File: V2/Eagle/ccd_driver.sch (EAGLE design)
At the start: 117 parts, among them J3 POWER_JACK, Q1 1A/60V/2.4Ω, Q2 BC214, Q3 2N2222, U10 TPD4S012DRYR, U11 0ZCJ0050FF2G, U12 REF3025AIDBZR, U13 DMP6023LE-13, U14 LMR23630, U2 MK02FN128VLF10, U4 ADS7946SRTER, U5 CP2102N-A01-GQFN20R, U8 S602TSRP

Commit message: modified power supply again. Added filter, ldo, and charge pump for analog rails. Created new schematic frame. General organization and minor changes
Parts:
- removed C110: 10uF, rcl:C-EUC0805
- removed C61, C62, C77: 100nF, SparkFun-Capacitors:10PF-50V-5%(0603)
- removed C69: 2.2uF, SparkFun-Capacitors:10PF-50V-5%(0603)
- removed C79: UWZ1C151MCL1GS, caps:UWZ1C151MCL1GS
- removed C88: 10uF, SparkFun-Capacitors:10PF-50V-5%(0603)
- removed C92: 47 pF, SparkFun-Capacitors:10PF-50V-5%(0603)
- removed C99: EMVE160ADA101MF55G, LM2776DBVR:EMVE160ADA101MF55G
- removed F3: 2920PTC, fuses:2920PTC
- removed J3: POWER_JACK, SparkFun-Connectors:POWER_JACK
- removed U12: REF3025AIDBZR, REF3025_DBZ-3:REF3025AIDBZR
- removed U8: S602TSRP, fuses:BT168GW
- added C18, C19, C25, C30, C45, C46, C48, C54: 10uF, eagle-ltspice:CC1206
- added C20, C21, C27, C35: 100nF, SparkFun-Capacitors:10PF-50V-5%(0603)
- added C22, C38, C53: UWZ1C151MCL1GS, caps:UWZ1C151MCL1GS
- added C24, C55: 1uF, SparkFun-Capacitors:10PF-50V-5%(0603)
- added C26, C28, C29, C33, C47: 2.2uF, rcl:C-EUC0805
- added C32: 10uF, SparkFun-Capacitors:10PF-50V-5%(0603)
- added C34: 10uF, rcl:C-EUC0805
- added C39: 0.47uF, SparkFun-Capacitors:10PF-50V-5%(0603)
- added C40: 4.7uF, SparkFun-Capacitors:10PF-50V-5%(0603)
- added C41: 2.2uF, SparkFun-Capacitors:10PF-50V-5%(0603)
- added C43: UWT1H101MNL1GS, UWT1H101MNL1GS:UWT1H101MNL1GS
- added C49, C50: EMVE160ADA101MF55G, caps:UWZ1C151MCL1GS
- added C51, C52, C56: 22uF, rcl:C-EUC0805
- added F5: 2920PTC, fuses:2920PTC
- added JACK1: JACK-C-PC-10A-RA(R), con-dcjack:JACK-C-PC-10A-RA(R)
- added JP4: (no value), pinhead:PINHD-1X2
- added L3: CIGW252010GLR47MNE, LM2776DBVR:CIGW252010GLR47MNE
- added R32, R47: 0, audio amplifier example:R-US_R0603
- added R33, R34: 51k, audio amplifier example:R-US_R0603
- added SUPPLY21: 2PT_GND_TIE, SparkFun-PowerSymbols:2PT_GND_TIE
- added T2: BC846, transistor:BC846
- added TP2: TPPAD1-13, testpad:TPPAD1-13
- added U$: LM2776DBVR, LM2776DBVR:LM2776DBVR
- added U1: S602TSRP, fuses:BT168GW
- added U3: REF3025AIDBZR, REF3025_DBZ-3:REF3025AIDBZR
- added U6: L5150BNTR, L5150BNTR:L5150BNTR
- C17: value 10uF -> UWT1H101MNL1GS; device eagle-ltspice:CC1206 -> UWT1H101MNL1GS:UWT1H101MNL1GS; CAPACITANCE (none) -> 100uF; PARTNO 490-12456-1-ND -> (none)
- CR1: ESD (none) -> 30kV; PEAKPOWER (none) -> 400W
- F6: IHOLD 1A -> 3A; PARTNO 2920L100 -> 2920L300
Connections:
- removed net N$25: F3.P$1, U13.D
- removed net N$5: C17.1, D4.A, R31.2, U8.G
- new net N$27: F5.P$1, U13.D
- new net N$34: C19.1, D4.A, R31.2, U1.G
- new net N$35: C45.1, R32.1, U6.IN
- new net N$36: L3.2, R32.2
- new net N$38: C25.1, R33.1, R34.2, T2.B
- new net N$39: C27.1, L3.1, T2.E
- new net N$4: C17.11, CR1.2, F5.P$2, JP4.2
- new net N$67: C48.1, R47.1, R54.1, U14.VIN
- new net N$93: C24.1, U$.C1+
- new net N$94: C24.2, U$.C1-
- new net V+: C20.1, C28.1, C29.1, C46.1, U$.EN, U$.VIN, U3.IN, U6.OUT
- new net V-: C26.1, U$.VOUT
- net +VIN: now also C18.1, C43.11, R33.2, R47.2, T2.C, U1.A; no longer C110.1, R54.1, U14.VIN, U8.A
- net 3.3V: now also R51.1; no longer C61.1, U12.IN
- net AGND: now also C20.2, C21.2, C26.2, C28.2, C29.2, C45.2, C46.2, SUPPLY21.P$1, U$.GND, U3.GND, U6.GND
- net GND: now also C17.22, C18.2, C19.2, C22.22, C25.2, C27.2, C33.2, C43.22, C48.2, C49.22, C51.2, C52.2, JACK1.2, R34.1, SUPPLY21.P$2, U1.K; no longer C110.2, C17.2, C61.2, C62.2, C69.2, C77.2, C79.22, C88.2, C99.11, J3.GND, J3.GNDBREAK, U12.GND, U8.K
- net N$14: now also JACK1.1, JP4.1, TP2.TP; no longer CR1.2, F3.P$2, J3.PWR
- net N$61: now also C33.1; no longer C69.1
- net N$70: no longer C92.2
- net N$88: now also C22.11, C51.1, C52.1; no longer C77.1, C79.11, C88.1, C92.1, R51.1
- net N$95: now also C49.11; no longer C99.22
- net VREF: now also C21.1, U3.OUT; no longer C62.1, U12.OUT
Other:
- note added: "+2.5V Ref"
- note added: "+5VA"
- note added: "-5VA"
- note added: "1.8" TFT Screen"
- note added: "3.3V Buck"
- note added: "5-36V Jack Input"
- note added: "Each peltier is seperatly fuesd"
- note added: "Encoder with pushbutton and LEDs"
- note added: "RC Filter W/ Bypass Transistor"
- note added: "Star Grounding"
- note added: "TODO: Add low ripple analog voltage [X]"
- note added: "TODO: Add negative rail [X]"
- note added: "TODO: Cosoldate all nets, pick pins on microcontroller"
- note added: "TODO: Fix amplifier, add unity gain amp, add filters"
- note added: "USB-B Micro"
- note removed: "5-36V Tolerant Input, 3.3V Out"
- note removed: "CCD & Amp"
- note removed: "CCD + AMP"
- note removed: "Main Microcontroller"
- note removed: "Peltier Cooler Driver"
- note removed: "Peltier Cooler Driver + Thermistor + Fan"
- note removed: "Power"
- note removed: "Precision 3V voltage ref"
- note removed: "SD Card"
- note removed: "TFT Screen + Encoder"
- note removed: "TFT-Screen + Encoder"
- note removed: "TODO: Add low ripple analog voltage"
- note removed: "TODO: Add negative rail"
- note removed: "TODO: Fix amplifier, add unity gain amp"
- note removed: "USB"

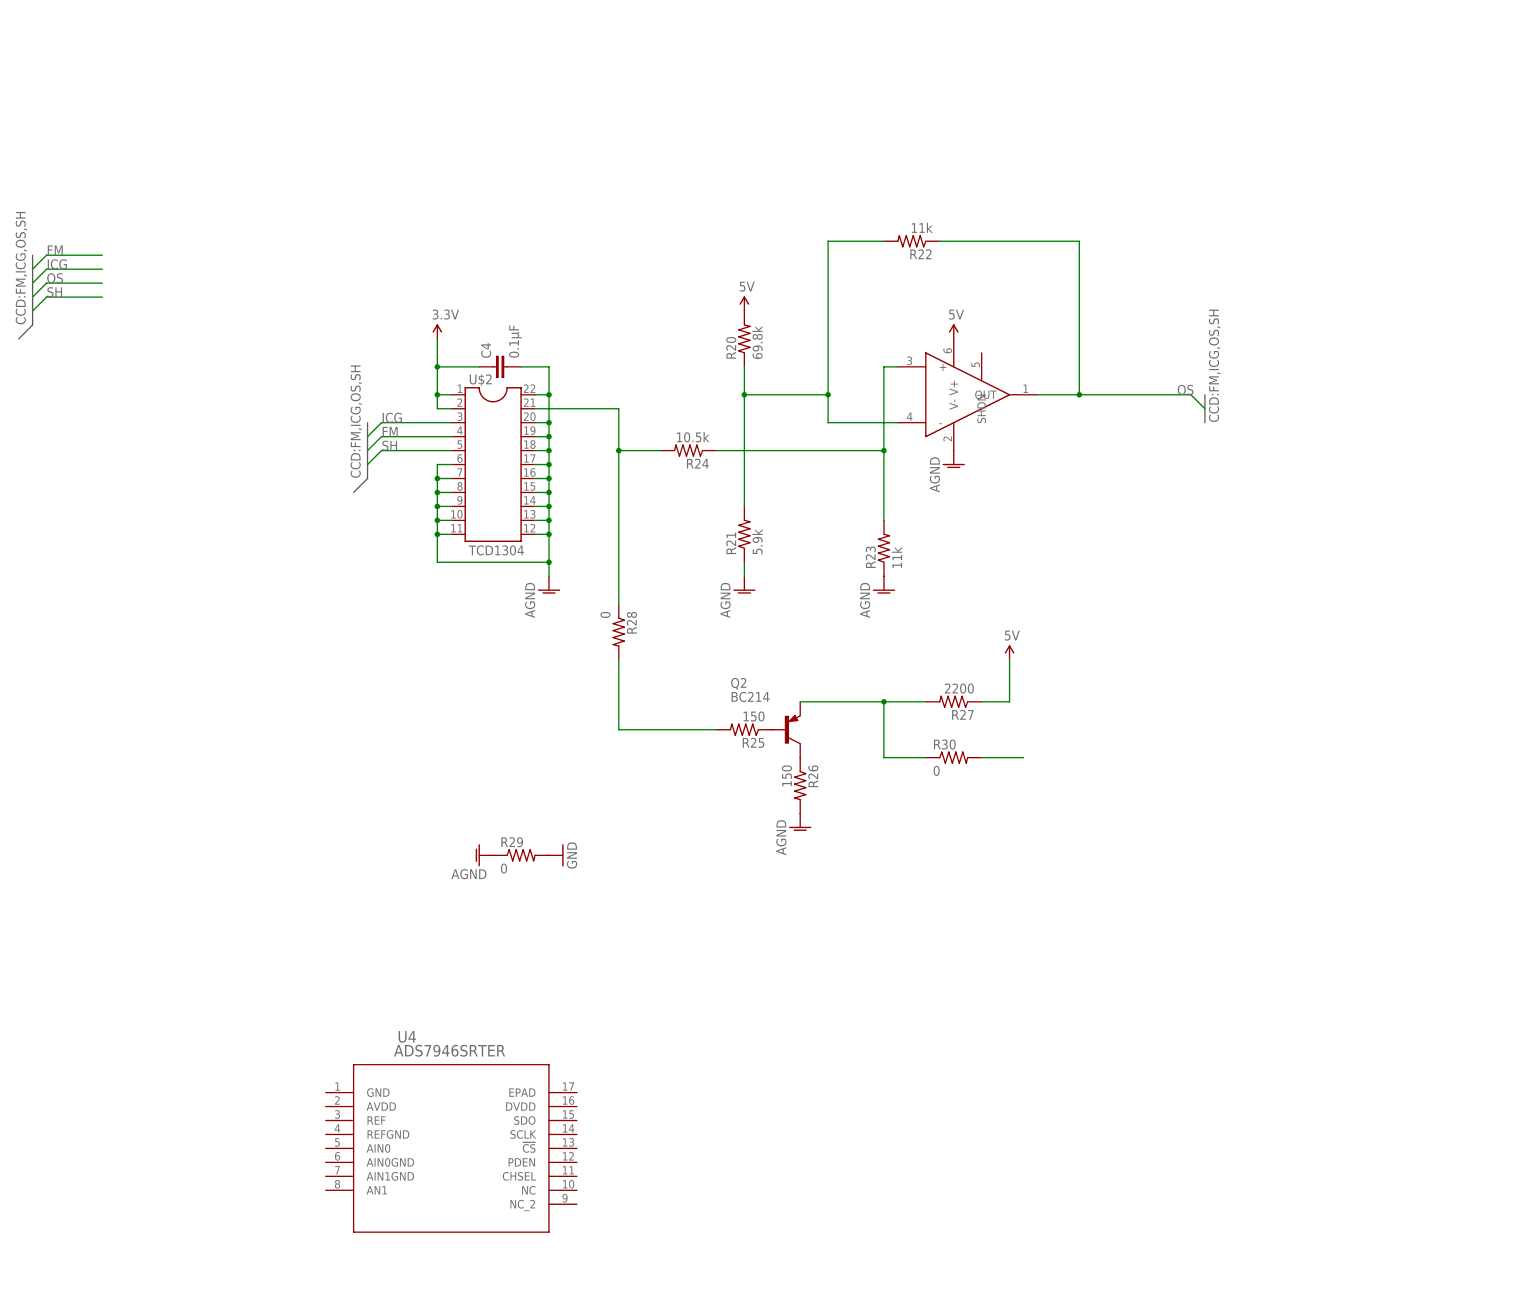
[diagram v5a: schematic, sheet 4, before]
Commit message: made matlab script to autocalculate amplifier resistor values
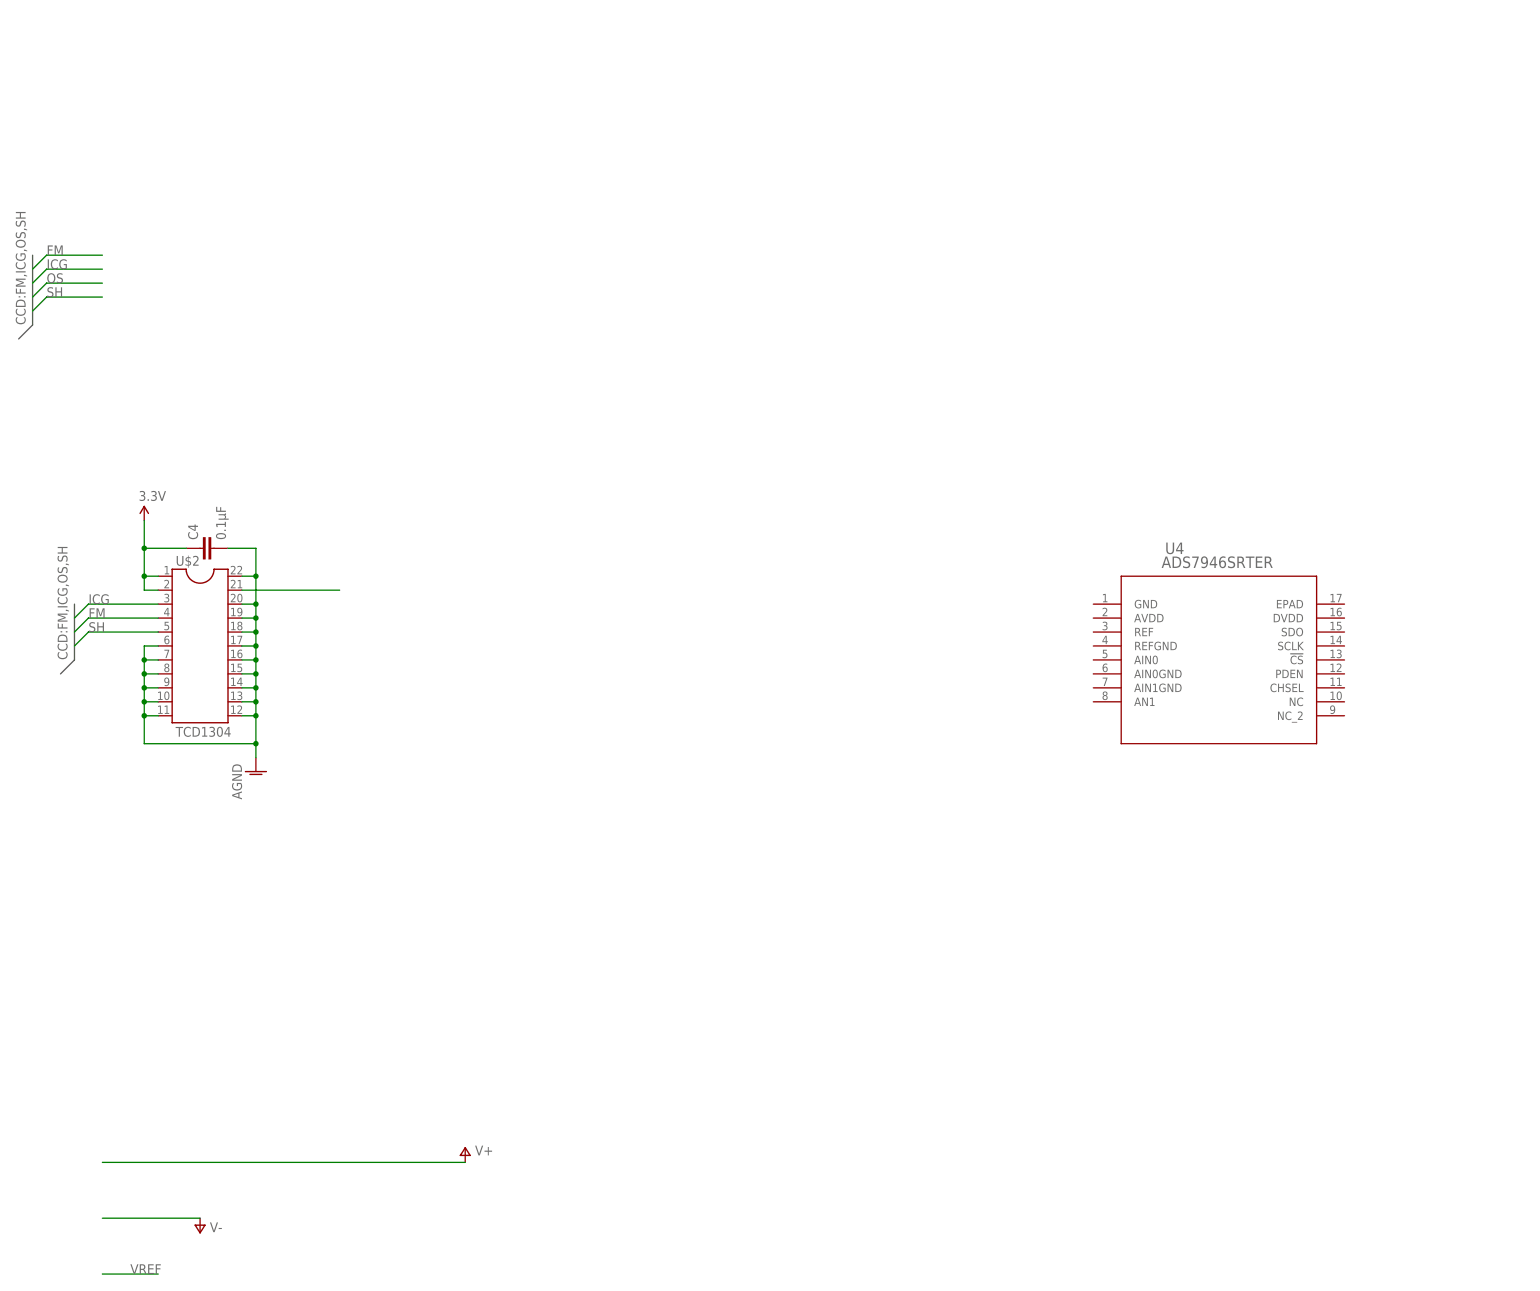
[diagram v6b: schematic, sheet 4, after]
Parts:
- removed Q2: BC214, transistor-pnp:BC214
- removed R20: 69.8k, resistor:R-US_R0805
- removed R21: 5.9k, resistor:R-US_R0805
- removed R22, R23: 11k, resistor:R-US_R0805
- removed R24: 10.5k, resistor:R-US_R0805
- removed R25, R26: 150, resistor:R-US_R0805
- removed R27: 2200, resistor:R-US_R0805
- removed R28, R29, R30: 0, resistor:R-US_R0805
- removed U$5: LTC6252, ccd:LTC6252
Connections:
- removed net 5V: R20.2, R27.1, U$5.V+
- removed net BU1: Q2.E, R27.2, R30.1
- removed net N$28: R23.2, R24.1, U$5.+
- removed net N$29: R24.2, R28.1, U$2.21
- removed net N$30: Q2.B, R25.1
- removed net N$31: Q2.C, R26.1
- removed net N$32: R25.2, R28.2
- removed net N$6: R20.1, R21.2, R22.2, U$5.-
- removed net OS: R22.1, R30.2, U$5.OUT
- new net N$5: U$2.21
- net AGND: no longer R21.1, R23.1, R26.2, R29.1, U$5.V-
- net GND: no longer R29.2
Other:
- moved on the sheet: C4, U$2, U4

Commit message: added new amp circuit for CCD
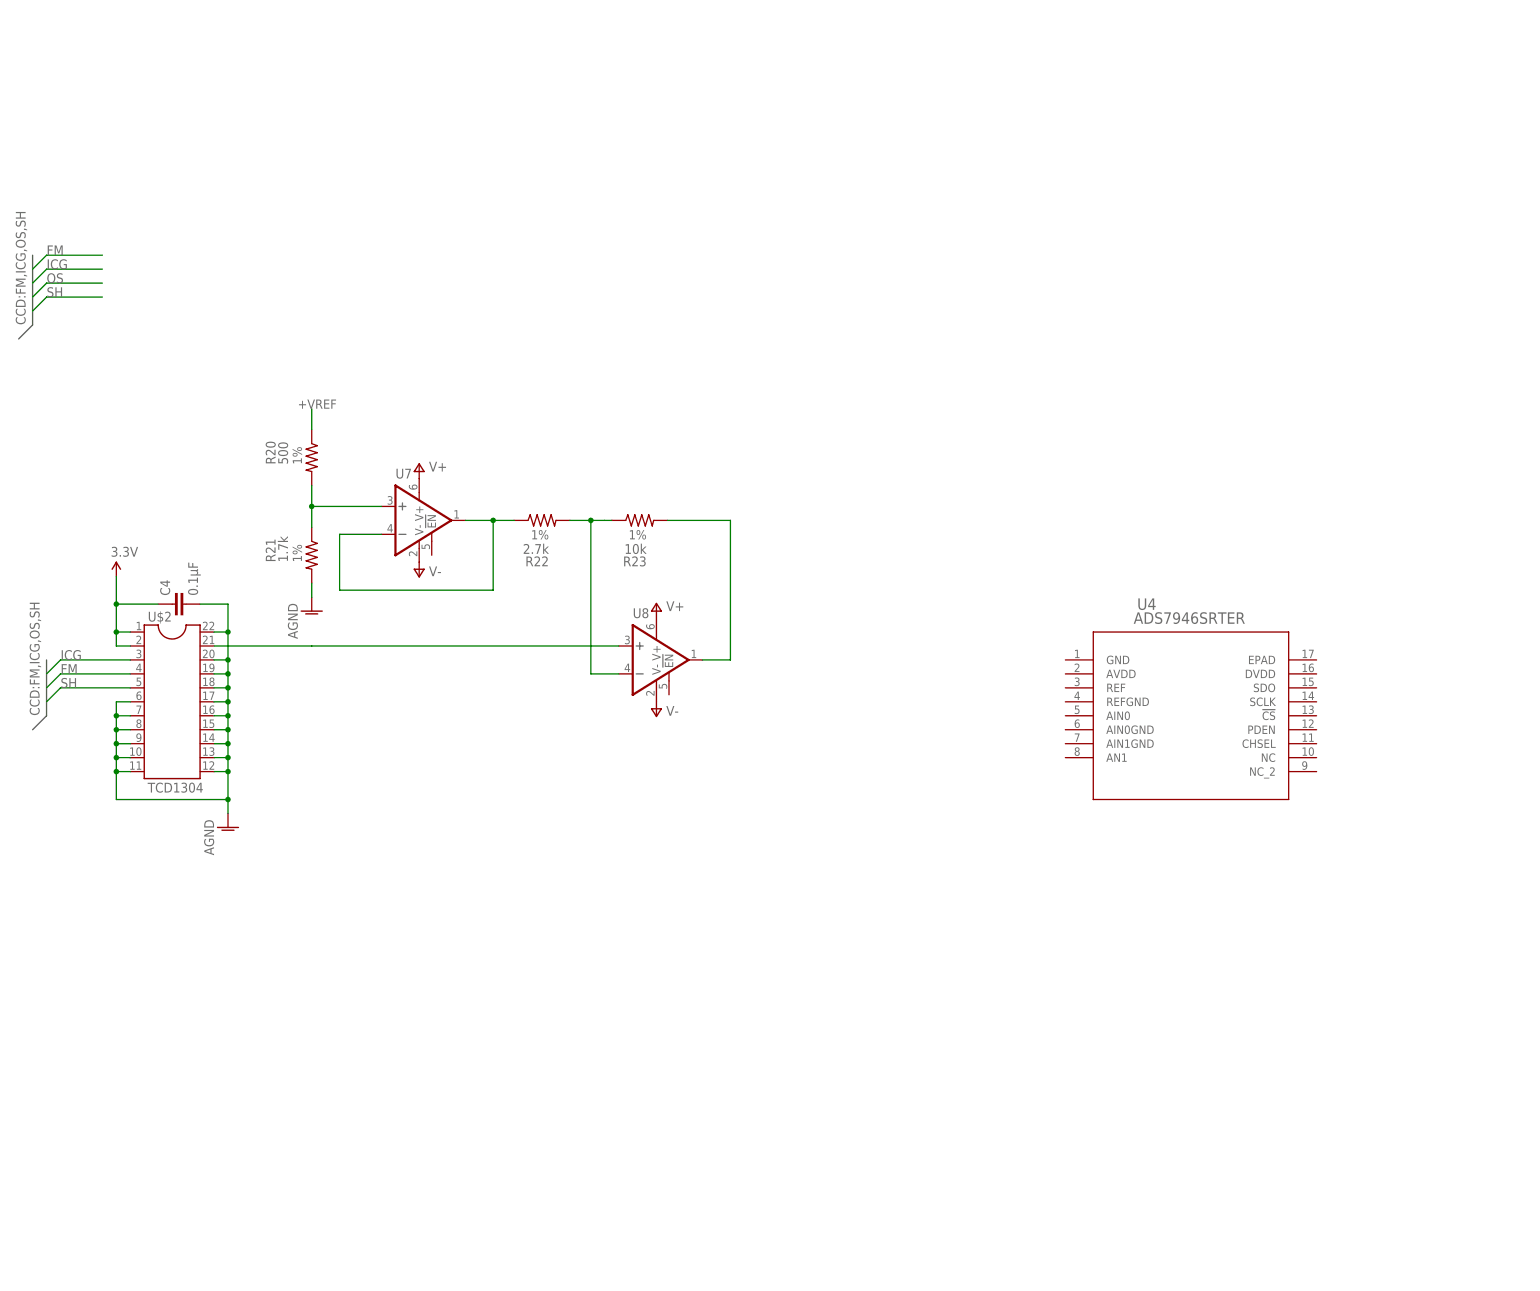
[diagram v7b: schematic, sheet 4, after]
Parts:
- added R20: 500, audio amplifier example:R-US_R0603
- added R21: 1.7k, audio amplifier example:R-US_R0603
- added R22: 2.7k, audio amplifier example:R-US_R0603
- added R23: 10k, audio amplifier example:R-US_R0603
- added U7, U8: ADA4807-1ARJZ-R2, ADA4807:ADA4807-1ARJZ-R2
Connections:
- new net +VREF: R20.1
- new net N$25: R22.1, U7.-IN, U7.OUT
- new net N$28: R22.2, R23.1, U8.-IN
- new net N$29: R23.2, U8.OUT
- new net N$6: R20.2, R21.1, U7.+IN
- net AGND: now also R21.2
- net N$5: now also U8.+IN
- net V+: now also U7.V+, U8.V+
- net V-: now also U7.V-, U8.V-
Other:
- moved on the sheet: C4, U$2, U4

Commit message: added filtering to analog section
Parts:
- added C23, C31: 820pF, SparkFun-Capacitors:10PF-50V-5%(0603)
- added C36: 100pF, SparkFun-Capacitors:10PF-50V-5%(0603)
- added C37: 10pF, SparkFun-Capacitors:10PF-50V-5%(0603)
- added R24: 857, audio amplifier example:R-US_R0603
- added R25: 1.15k, audio amplifier example:R-US_R0603
- added R26: 105, audio amplifier example:R-US_R0603
- added R27: 2.67k, audio amplifier example:R-US_R0603
- added U12, U9: ADA4807-1ARJZ-R2, ADA4807:ADA4807-1ARJZ-R2
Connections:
- new net N$30: C23.2, C31.1, R24.1
- new net N$31: C31.2, R25.1, U9.+IN
- new net N$32: R24.2, R26.1, U9.-IN, U9.OUT
- new net N$40: C37.2, R27.2, U12.+IN
- new net N$41: C36.1, R26.2, R27.1
- new net N$42: C36.2, U12.-IN, U12.OUT
- net AGND: now also C37.1, R25.2
- net N$29: now also C23.1
- net V+: now also U12.V+, U9.V+
- net V-: now also U12.V-, U9.V-
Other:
- note added: "2nd Order High Pass Bessel 250kHz Passband 10kHz -40dB Stopband"
- note added: "2nd Order Low Pass Butterworth Bessel 8MHz Passband 30MHz -20dB Stopband"
- note added: "Input : 0.8 - 2.5V Output: -5 - +5V"
- note added: "TODO: Add filters [X] Maybe check these"
- note added: "TODO: Fix amplifier [X]"
- note removed: "TODO: Fix amplifier, add unity gain amp, add filters"
- moved on the sheet: R20, R21, R22, R23, U4, U7, U8
